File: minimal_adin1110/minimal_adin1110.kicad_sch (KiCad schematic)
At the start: 32 parts, among them U6 ADIN1110CCPZ, Y1 FA-128 25.0000MF20X-K0

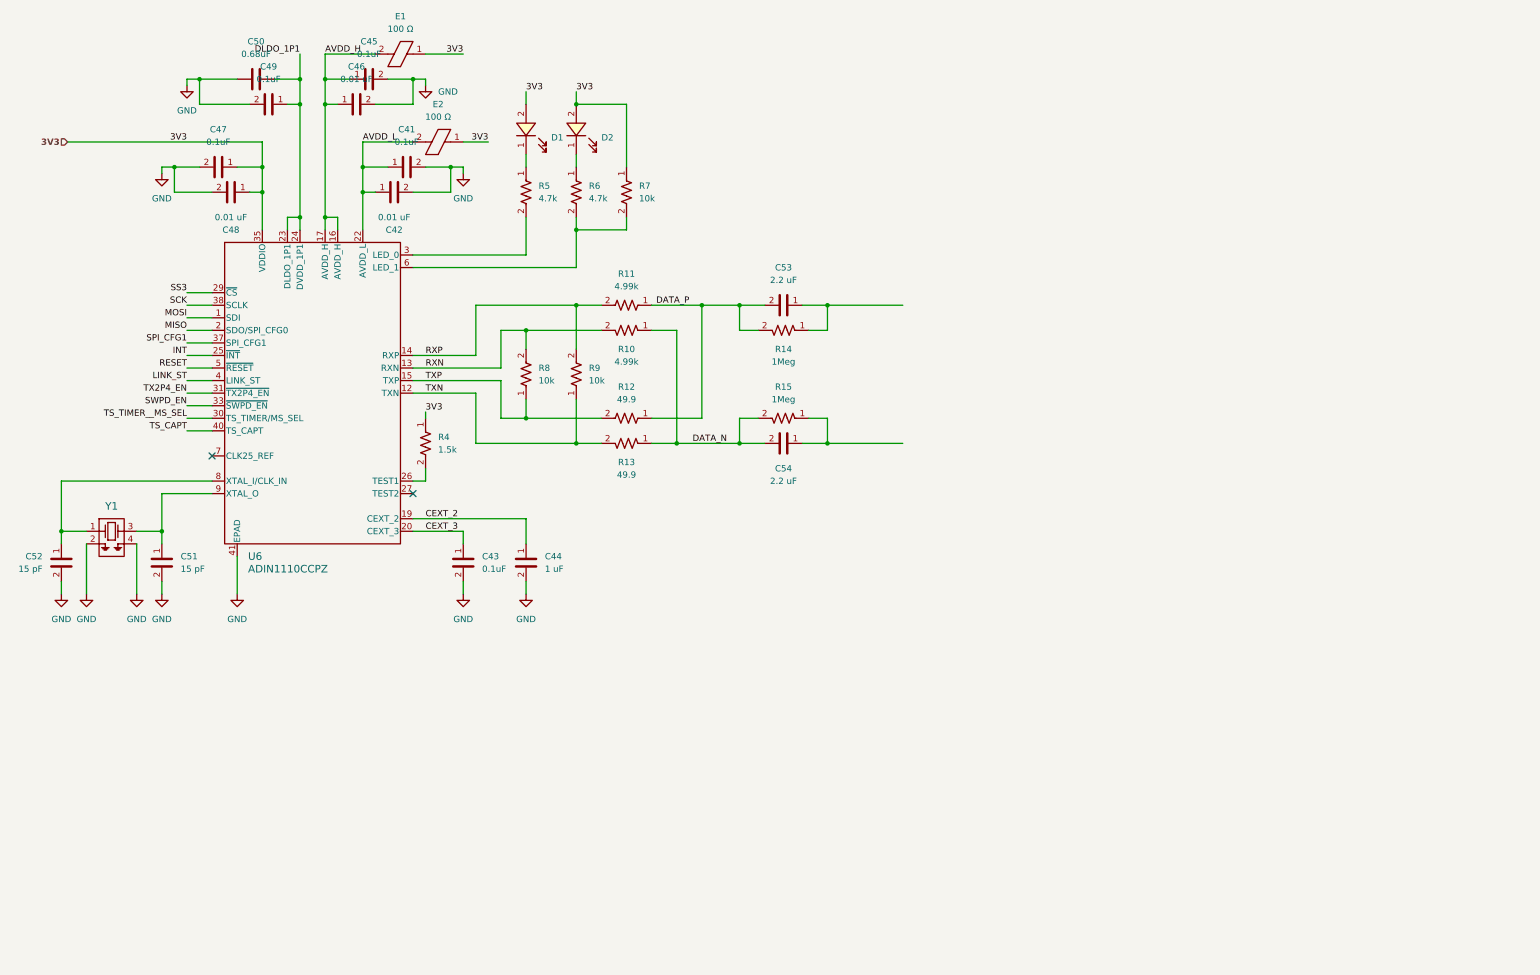
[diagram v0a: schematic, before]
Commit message: Add VRML file reference for minimal_adin1110 project
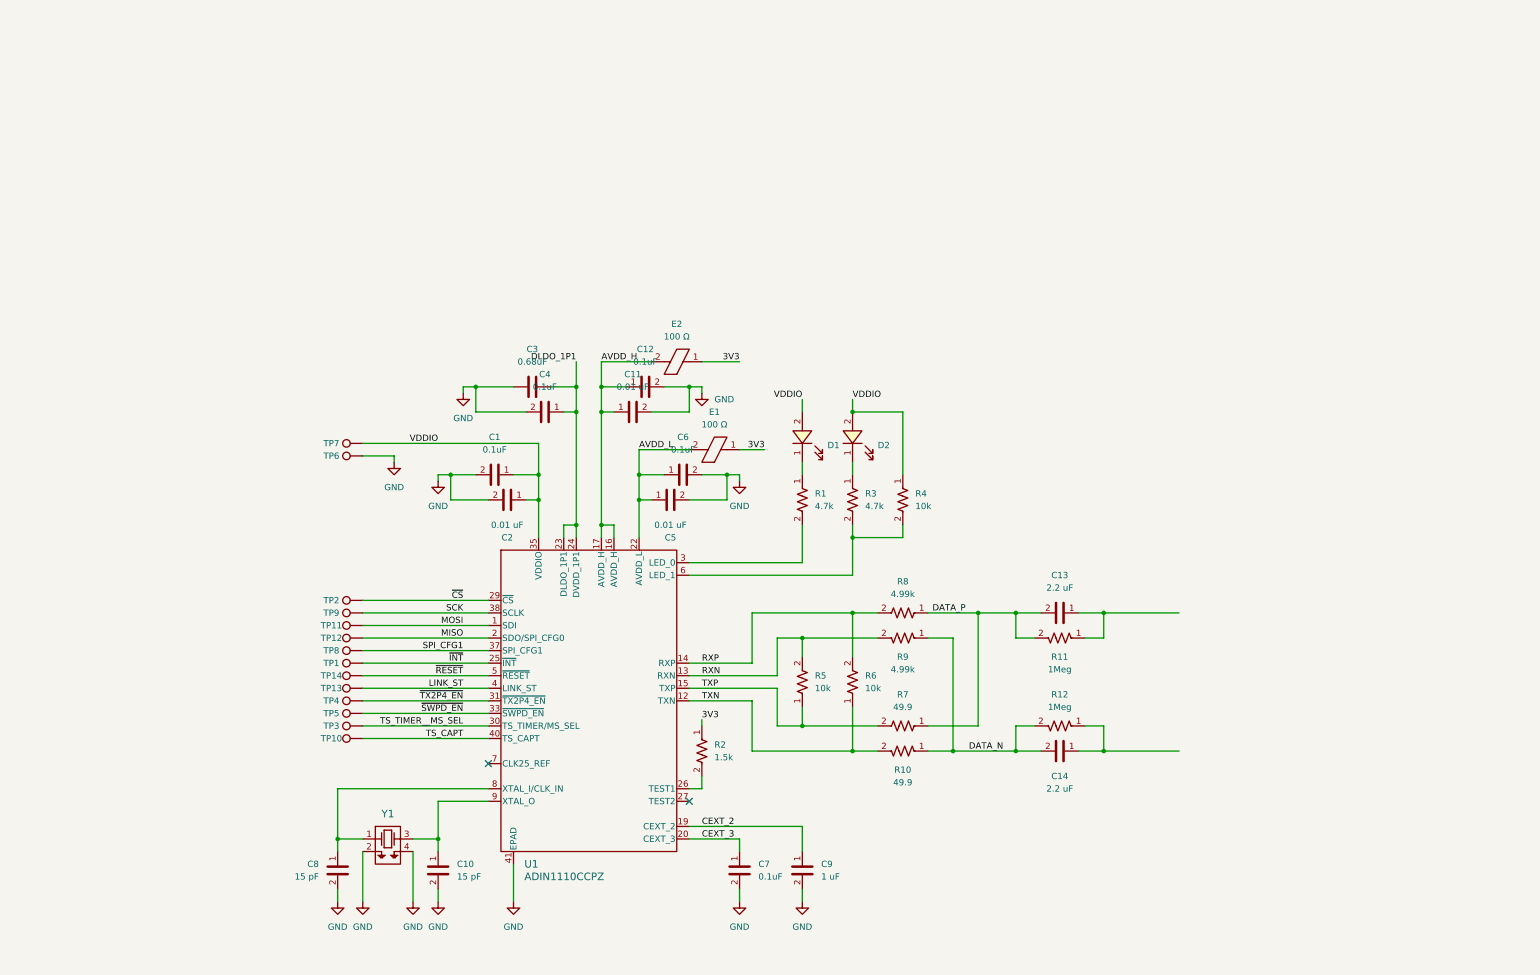
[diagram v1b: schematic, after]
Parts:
- added TP1, TP10, TP11, TP12, TP13, TP14, TP2, TP3, TP4, TP5, TP6, TP7, TP8, TP9: TestPoint, test_point_footprints:TestPoint_THTPad_Castelated, symbol UNITED_TEST_POINTS:TestPoint_Castelated
- renumbered C47 to C1, C51 to C10, C46 to C11, C45 to C12, C53 to C13, C54 to C14, C48 to C2, C50 to C3, C49 to C4, C42 to C5, C41 to C6, C43 to C7, C52 to C8, C44 to C9, E2 to E1, E1 to E2, R5 to R1, R13 to R10, R14 to R11, R15 to R12, R4 to R2, R6 to R3, R7 to R4, R8 to R5, R9 to R6, R12 to R7, R11 to R8, R10 to R9, U6 to U1
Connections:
- net 3V3: no longer C1.1, C2.1, D1.2, D2.2, R4.1, U1.35 (VDDIO)
- net GND: now also TP6.1
- net LINK_ST: now also TP13.1
- net MISO: now also TP12.1
- net MOSI: now also TP11.1
- net SCK: now also TP9.1
- net SPI_CFG1: now also TP8.1
- net TS_CAPT: now also TP10.1
- net TS_TIMER__MS_SEL: now also TP3.1
- net INT renamed ~{INT}
- net ~{INT}: now also TP1.1
- net RESET renamed ~{RESET}
- net ~{RESET}: now also TP14.1
- net SS3 renamed ~{CS}
- net ~{CS}: now also TP2.1
- net SWPD_EN renamed ~{SWPD_EN}
- net ~{SWPD_EN}: now also TP5.1
- net TX2P4_EN renamed ~{TX2P4_EN}
- net ~{TX2P4_EN}: now also TP4.1
- new net VDDIO: C1.1, C2.1, D1.2, D2.2, R4.1, TP7.1, U1.35 (VDDIO)
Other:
- moved on the sheet: C1, C10, C11, C12, C13, C14, C2, C3, C4, C5, C6, C7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

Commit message: Backup
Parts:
- added J1, J2, J3: CLP-102-02-G-D-BE, connector_footprints:CLP-102-02-G-D-BE, symbol UNITED_CONNECTORS_DATA_BASE:J_CLP-102-02-G-D-BE
- added J4: CLP-112-02-G-D-BE, connector_footprints:CLP-114-02-G-D-BE, symbol UNITED_CONNECTORS_DATA_BASE:J_CLP-114-02-G-D-BE
- added JP1, JP2, JP3: SolderJumper_3_Open, solder_jumper_footprints:SolderJumper-3_P1.3mm_Open_RoundedPad1.0x1.5mm_NumberLabels, symbol UNITED_SOLDER_JUMPERS:SolderJumper_3_Open
- added TP15, TP16, TP17, TP18, TP19, TP20: TestPoint, test_point_footprints:TestPoint_THTPad_Castelated, symbol UNITED_TEST_POINTS:TestPoint_Castelated
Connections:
- net DLDO_1P1: now also JP3.1 (A); no longer C3.1, U1.24 (DVDD_1P1)
- net GND: now also J1.2, J1.4, J2.2, J2.4, J3.2, J3.4, J4.1, J4.11, J4.13, J4.15, J4.17, J4.18, J4.19, J4.21, J4.23, J4.25, J4.27, J4.3, J4.5, J4.7, J4.9, TP17.1, TP18.1, TP20.1
- net LINK_ST: now also J4.4
- net MISO: now also J4.6
- net MOSI: now also J4.8
- net SCK: now also J4.12
- net SPI_CFG1: now also J4.14
- net TS_CAPT: now also J4.10
- net TS_TIMER__MS_SEL: now also J4.24
- net VDDIO: now also R2.1, J4.16, JP1.1 (A), JP2.1 (A)
- net ~{CS}: now also J4.26
- net ~{INT}: now also J4.28
- net ~{RESET}: now also J4.2
- net ~{SWPD_EN}: now also J4.20
- net ~{TX2P4_EN}: now also J4.22
- removed net 3V3: E1.1, E2.1, R2.1
- new net 1P1_EXT: J3.1, J3.3, JP3.3 (B), TP19.1
- new net AVDD_H_EXT: J1.1, J1.3, JP2.3 (B), TP15.1
- new net AVDD_H_IN: E2.1, JP2.2 (C)
- new net AVDD_L_EXT: J2.1, J2.3, JP1.3 (B), TP16.1
- new net AVDD_L_IN: E1.1, JP1.2 (C)
- new net DVDD_1P1: C3.1, JP3.2 (C), U1.24 (DVDD_1P1)
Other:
- moved on the sheet: C11, C12, C3, C4, D1, D2, E1, E2, R1, R3, R4, TP6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

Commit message: Backup
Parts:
- added J5: CLP-102-02-G-D-BE, connector_footprints:CLP-102-02-G-D-BE, symbol UNITED_CONNECTORS_DATA_BASE:J_CLP-102-02-G-D-BE
- added TP21, TP22: TestPoint, test_point_footprints:TestPoint_THTPad_Castelated, symbol UNITED_TEST_POINTS:TestPoint_Castelated
- C3: value 0.68uF -> 680 nF; footprint footprints:C_0402_1005Metric -> capacitor_footprints:C_0402_1005Metric; symbol CAPACITORS:C_000005 -> UNITED_CAPACITORS_DATA_BASE:C_GCM155C71A684KE38D; Case Code - in (none) -> 0402; Case Code - mm (none) -> 1005; Dielectric (none) -> X7S; Manufacturer (none) -> Murata Electronics; Series (none) -> GCM155C71A; Symbol Name (none) -> C_GCM155C71A684KE38D; Tolerance (none) -> 10%; Trustedparts Search (none) -> https://www.trustedparts.com/en/search/GCM155C71A684KE38D; Voltage Rating (none) -> 10V
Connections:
- net DATA_AND_POWER_P: now reaches C13.1, R11.1
- net DATA_AND_POWER_P: now also J5.1, J5.3, TP21.1
- net DATA_AND_POWER_N: now reaches C14.1, R12.1
- net DATA_AND_POWER_N: now also J5.2, J5.4, TP22.1
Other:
- moved on the sheet: C11, C12

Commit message: Add UNITED_MOUSE_BITES_DATA_BASE library to sym-lib-table
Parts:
- added MB1: mouse-bite-midle-50mil-200mil, mouse_bite_footprints:mouse-bite-50mil-790mil, symbol UNITED_MOUSE_BITES_DATA_BASE:mouse-bite-50mil-790mil
- added MB2, MB3, MB4, MB5: mouse-bite-midle-50mil-200mil, mouse_bite_footprints:mouse-bite-midle-50mil-200mil, symbol UNITED_MOUSE_BITES_DATA_BASE:mouse-bite-midle-50mil-200mil
- renumbered C12 to C11, C11 to C12, C7 to C6, C6 to C7, J4 to J1, J3 to J2, J2 to J3, J1 to J4, JP3 to JP1, JP1 to JP2, JP2 to JP3, TP20 to TP15, TP19 to TP16, TP16 to TP18, TP18 to TP19, TP15 to TP20

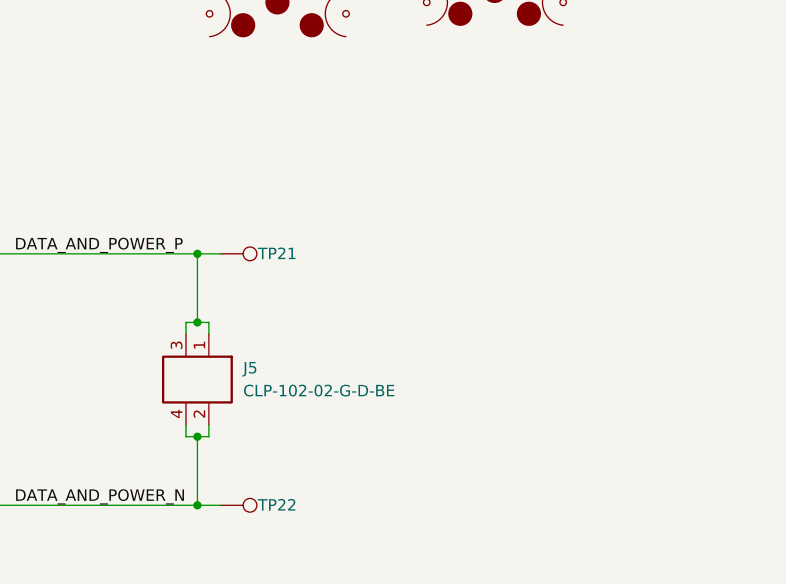
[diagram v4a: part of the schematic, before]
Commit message: Update component blacklist and add new libraries to symbol and footprint tables
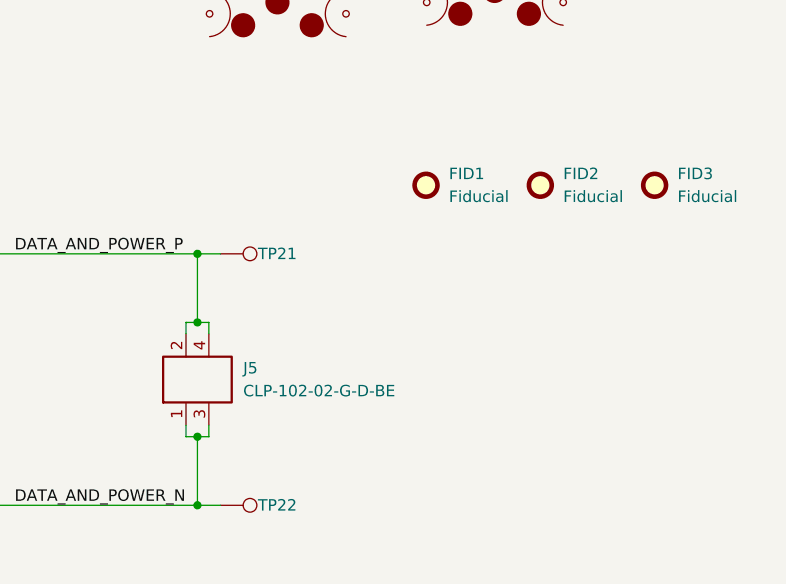
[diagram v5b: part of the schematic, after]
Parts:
- added FID1, FID2, FID3: Fiducial, no_components_footprints:Fiducial_0.5mm_Mask1mm, symbol UNITED_NO_COMPONENTS_DATA_BASE:Fiducial
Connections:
- net DATA_AND_POWER_N: now also J5.1, J5.3; no longer J5.2, J5.4
- net DATA_AND_POWER_P: now also J5.2, J5.4; no longer J5.1, J5.3
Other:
- moved on the sheet: J5
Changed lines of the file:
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@@
 	)
 	(symbol
+		(lib_id "UNITED_NO_COMPONENTS_DATA_BASE:Fiducial")
+		(at 381 127 0)
+		(unit 1)
+		(exclude_from_sim no)
+		(in_bom yes)
+		(on_board yes)
+		(dnp no)
+		(fields_autoplaced yes)
+		(property "Reference" "FID3"
+			(at 383.54 125.7299 0)
+			(effects
+				(font
+					(size 1.27 1.27)
+				)
+				(justify left)
+			)
+		)
+		(property "Value" "Fiducial"
+			(at 383.54 128.2699 0)
+			(effects
+				(font
+					(size 1.27 1.27)
+				)
+				(justify left)
+			)
+		)
+		(property "Footprint" "no_components_footprints:Fiducial_0.5mm_Mask1mm"
+			(at 381 134.62 0)
+			(effects
+				(font
+					(size 1.27 1.27)
+				)
+				(justify left)
+				(hide yes)
+			)
+		)
+		(property "Datasheet" "~"
+			(at 381 129.54 0)
+			(effects
+				(font
+					(size 1.27 1.27)
+				)
+				(justify left)
+				(hide yes)
+			)
+		)
+		(property "Description" "Fiducial Marker"
+			(at 381 132.08 0)
+			(effects
+				(font
+					(size 1.27 1.27)
+				)
+				(justify left)
+				(hide yes)
+			)
+		)
+		(instances
+			(project "minimal_adin1110"
+				(path "/26ddf1b8-aee4-468d-a26c-7bd63f3a2989"
+					(reference "FID3")
+					(unit 1)
+				)
+			)
+		)
+	)
+	(symbol
 		(lib_id "UNITED_IC_ADI:U_ADIN1110CCPZ")
 		(at 203.2 152.4 0)
@@
 	(symbol
 		(lib_id "UNITED_CONNECTORS_DATA_BASE:J_CLP-102-02-G-D-BE")
-		(at 330.2 148.59 270)
+		(at 330.2 148.59 90)
 		(unit 1)
 		(exclude_from_sim no)
@@
 					(size 1.27 1.27)
 				)
-				(justify left)
+				(justify right)
 			)
 		)
@@
 					(size 1.27 1.27)
 				)
-				(justify left)
+				(justify right)
 			)
 		)
 		(property "Footprint" "connector_footprints:CLP-102-02-G-D-BE"
-			(at 322.58 153.67 0)
+			(at 337.82 143.51 0)
 			(show_name yes)
 			(effects
@@
 		)
 		(property "Datasheet" "https://suddendocs.samtec.com/catalog_english/clp_sm.pdf?_gl=1*1y4jlr9*_gcl_au*MTM0MTYyNTQ5MS4xNzM2MDk5MTUz*_ga*MTYxNDYyMTQ0Mi4xNzM2MDk5MTUz*_ga_3KFNZC07WW*MTczNjY4MDQ4OS4xNS4xLjE3MzY2ODEzNzcuNjAuMC4w"
-			(at 320.04 153.67 0)
+			(at 340.36 143.51 0)
 			(show_name yes)
 			(effects
@@
 		)
 		(property "Description" "Samtec CLP-1xx-02-G-D-BE series,  2 positions connector,  1.27 mm pitch,  Black,  Vertical mounting,  5.2 A,  300 V,  Through Hole,  Tin plated"
-			(at 317.5 153.67 0)
+			(at 342.9 143.51 0)
 			(show_name yes)
 			(effects
@@
 		)
 		(property "Color" "Black"
-			(at 314.96 153.67 0)
+			(at 345.44 143.51 0)
 			(show_name yes)
 			(effects
@@
 		)
 		(property "Contact Plating" "Tin"
-			(at 312.42 153.67 0)
+			(at 347.98 143.51 0)
 			(show_name yes)
 			(effects
@@
 		)
 		(property "Current Rating (A)" "5.2"
-			(at 309.88 153.67 0)
+			(at 350.52 143.51 0)
 			(show_name yes)
 			(effects
@@
 		)
 		(property "MPN" "CLP-102-02-G-D-BE"
-			(at 307.34 153.67 0)
+			(at 353.06 143.51 0)
 			(show_name yes)
 			(effects
@@
 		)
 		(property "Manufacturer" "Samtec"
-			(at 304.8 153.67 0)
+			(at 355.6 143.51 0)
 			(show_name yes)
 			(effects
@@
 		)
 		(property "Mounting Angle" "Vertical"
-			(at 302.26 153.67 0)
+			(at 358.14 143.51 0)
 			(show_name yes)
 			(effects
@@
 		)
 		(property "Mounting Style" "Through Hole"
-			(at 299.72 153.67 0)
+			(at 360.68 143.51 0)
 			(show_name yes)
 			(effects
@@
 		)
 		(property "Number of Rows" "2"
-			(at 297.18 153.67 0)
+			(at 363.22 143.51 0)
 			(show_name yes)
 			(effects
@@
 		)
 		(property "Pin Count" "2"
-			(at 294.64 153.67 0)
+			(at 365.76 143.51 0)
 			(show_name yes)
 			(effects
@@
 		)
 		(property "Pitch (mm)" "1.27"
-			(at 292.1 153.67 0)
+			(at 368.3 143.51 0)
 			(show_name yes)
 			(effects
@@
 		)
 		(property "Series" "CLP-1xx-02-G-D-BE"
-			(at 289.56 153.67 0)
+			(at 370.84 143.51 0)
 			(show_name yes)
 			(effects
@@
 		)
 		(property "Symbol Name" "J_CLP-102-02-G-D-BE"
-			(at 287.02 153.67 0)
+			(at 373.38 143.51 0)
 			(show_name yes)
 			(effects
@@
 		)
 		(property "Trustedparts Search" "https://www.trustedparts.com/en/search/CLP-102-02-G-D-BE"
-			(at 284.48 153.67 0)
+			(at 375.92 143.51 0)
 			(show_name yes)
 			(effects
@@
 		)
 		(property "Voltage Rating (V)" "300"
-			(at 281.94 153.67 0)
+			(at 378.46 143.51 0)
 			(show_name yes)
 			(effects
@@
 	)
 	(symbol
+		(lib_id "UNITED_NO_COMPONENTS_DATA_BASE:Fiducial")
+		(at 368.3 127 0)
+		(unit 1)
+		(exclude_from_sim no)
+		(in_bom yes)
+		(on_board yes)
+		(dnp no)
+		(fields_autoplaced yes)
+		(property "Reference" "FID2"
+			(at 370.84 125.7299 0)
+			(effects
+				(font
+					(size 1.27 1.27)
+				)
+				(justify left)
+			)
+		)
+		(property "Value" "Fiducial"
+			(at 370.84 128.2699 0)
+			(effects
+				(font
+					(size 1.27 1.27)
+				)
+				(justify left)
+			)
+		)
+		(property "Footprint" "no_components_footprints:Fiducial_0.5mm_Mask1mm"
+			(at 368.3 134.62 0)
+			(effects
+				(font
+					(size 1.27 1.27)
+				)
+				(justify left)
+				(hide yes)
+			)
+		)
+		(property "Datasheet" "~"
+			(at 368.3 129.54 0)
+			(effects
+				(font
+					(size 1.27 1.27)
+				)
+				(justify left)
+				(hide yes)
+			)
+		)
+		(property "Description" "Fiducial Marker"
+			(at 368.3 132.08 0)
+			(effects
+				(font
+					(size 1.27 1.27)
+				)
+				(justify left)
+				(hide yes)
+			)
+		)
+		(instances
+			(project "minimal_adin1110"
+				(path "/26ddf1b8-aee4-468d-a26c-7bd63f3a2989"
+					(reference "FID2")
+					(unit 1)
+				)
+			)
+		)
+	)
+	(symbol
 		(lib_id "power:GND")
 		(at 175.26 107.95 0)
@@
 					(unit 1)
 				)
+			)
+		)
+	)
+	(symbol
+		(lib_id "UNITED_NO_COMPONENTS_DATA_BASE:Fiducial")
+		(at 355.6 127 0)
+		(unit 1)
+		(exclude_from_sim no)
+		(in_bom yes)
+		(on_board yes)
+		(dnp no)
+		(fields_autoplaced yes)
+		(property "Reference" "FID1"
+			(at 358.14 125.7299 0)
+			(effects
+				(font
+					(size 1.27 1.27)
+				)
+				(justify left)
+			)
+		)
+		(property "Value" "Fiducial"
+			(at 358.14 128.2699 0)
+			(effects
+				(font
+					(size 1.27 1.27)
+				)
+				(justify left)
+			)
+		)
+		(property "Footprint" "no_components_footprints:Fiducial_0.5mm_Mask1mm"
+			(at 355.6 134.62 0)
+			(effects
+				(font
+					(size 1.27 1.27)
+				)
+				(justify left)
+				(hide yes)
+			)
+		)
+		(property "Datasheet" "~"
+			(at 355.6 129.54 0)
+			(effects
+				(font
+					(size 1.27 1.27)
+				)
+				(justify left)
+				(hide yes)
+			)
+		)
+		(property "Description" "Fiducial Marker"
+			(at 355.6 132.08 0)
+			(effects
+				(font
+					(size 1.27 1.27)
+				)
+				(justify left)
+				(hide yes)
+			)
+		)
+		(instances
+			(project ""
+				(path "/26ddf1b8-aee4-468d-a26c-7bd63f3a2989"
+					(reference "FID1")
+					(unit 1)
+				)
